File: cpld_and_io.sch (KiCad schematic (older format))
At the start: 3 parts, among them U12 IS61LV5128AL-10TLI, U4 5M1270ZT144C5N

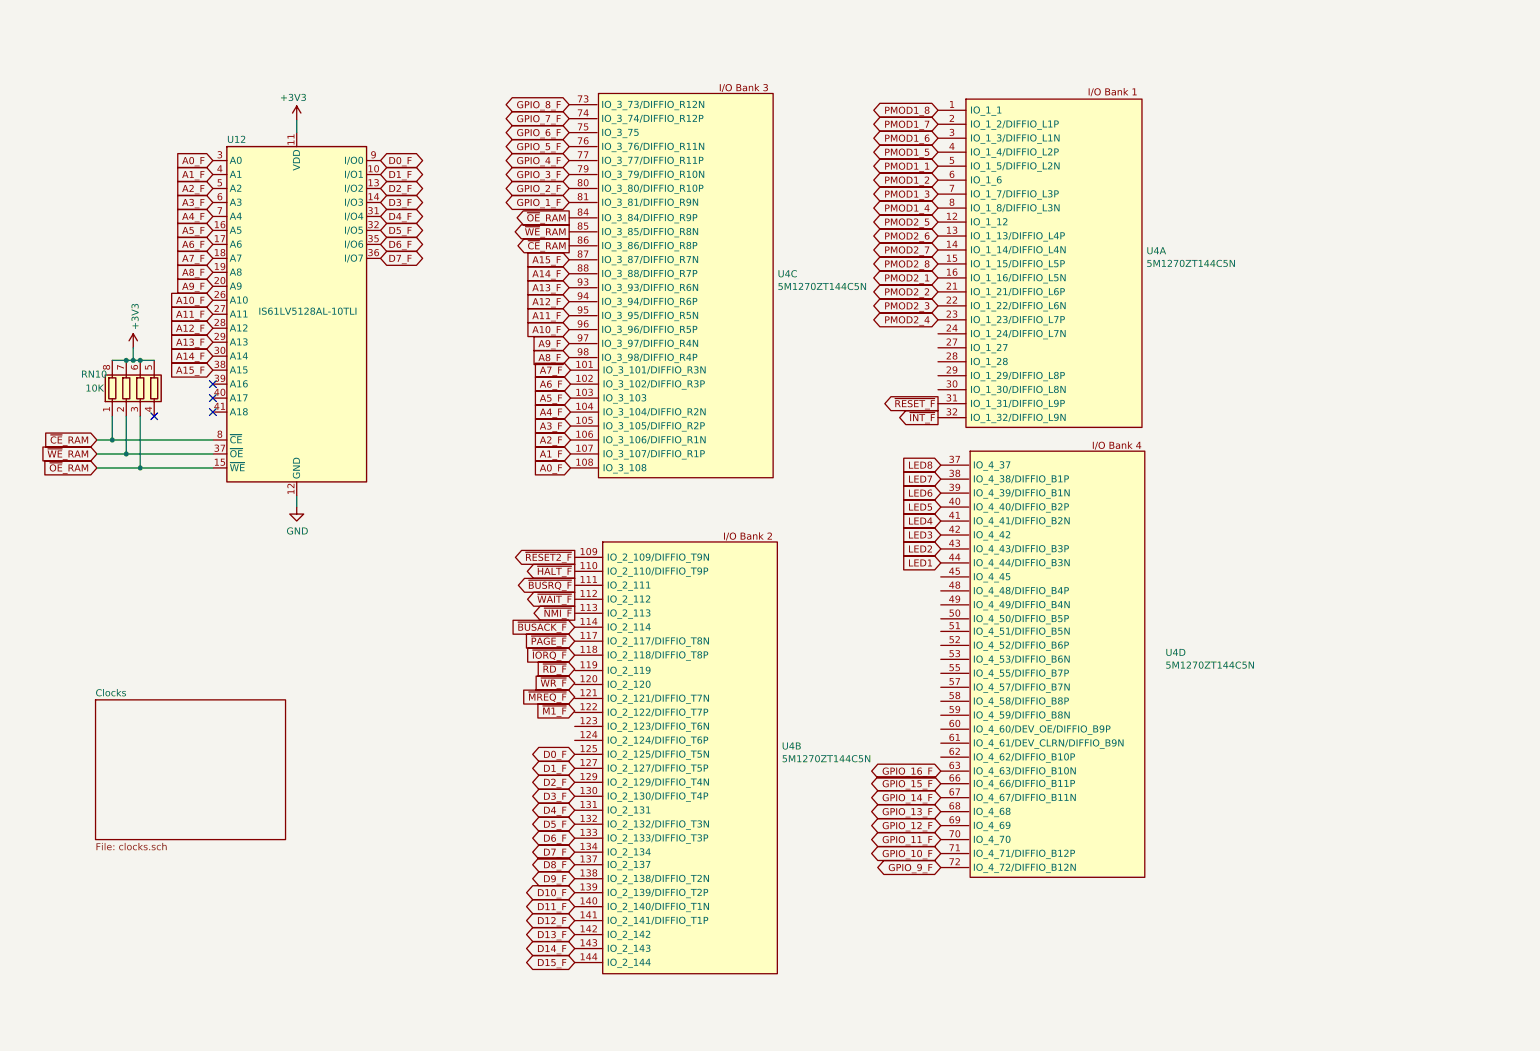
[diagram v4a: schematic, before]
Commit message: fixed errors, connected all pins, switched to 4 layers
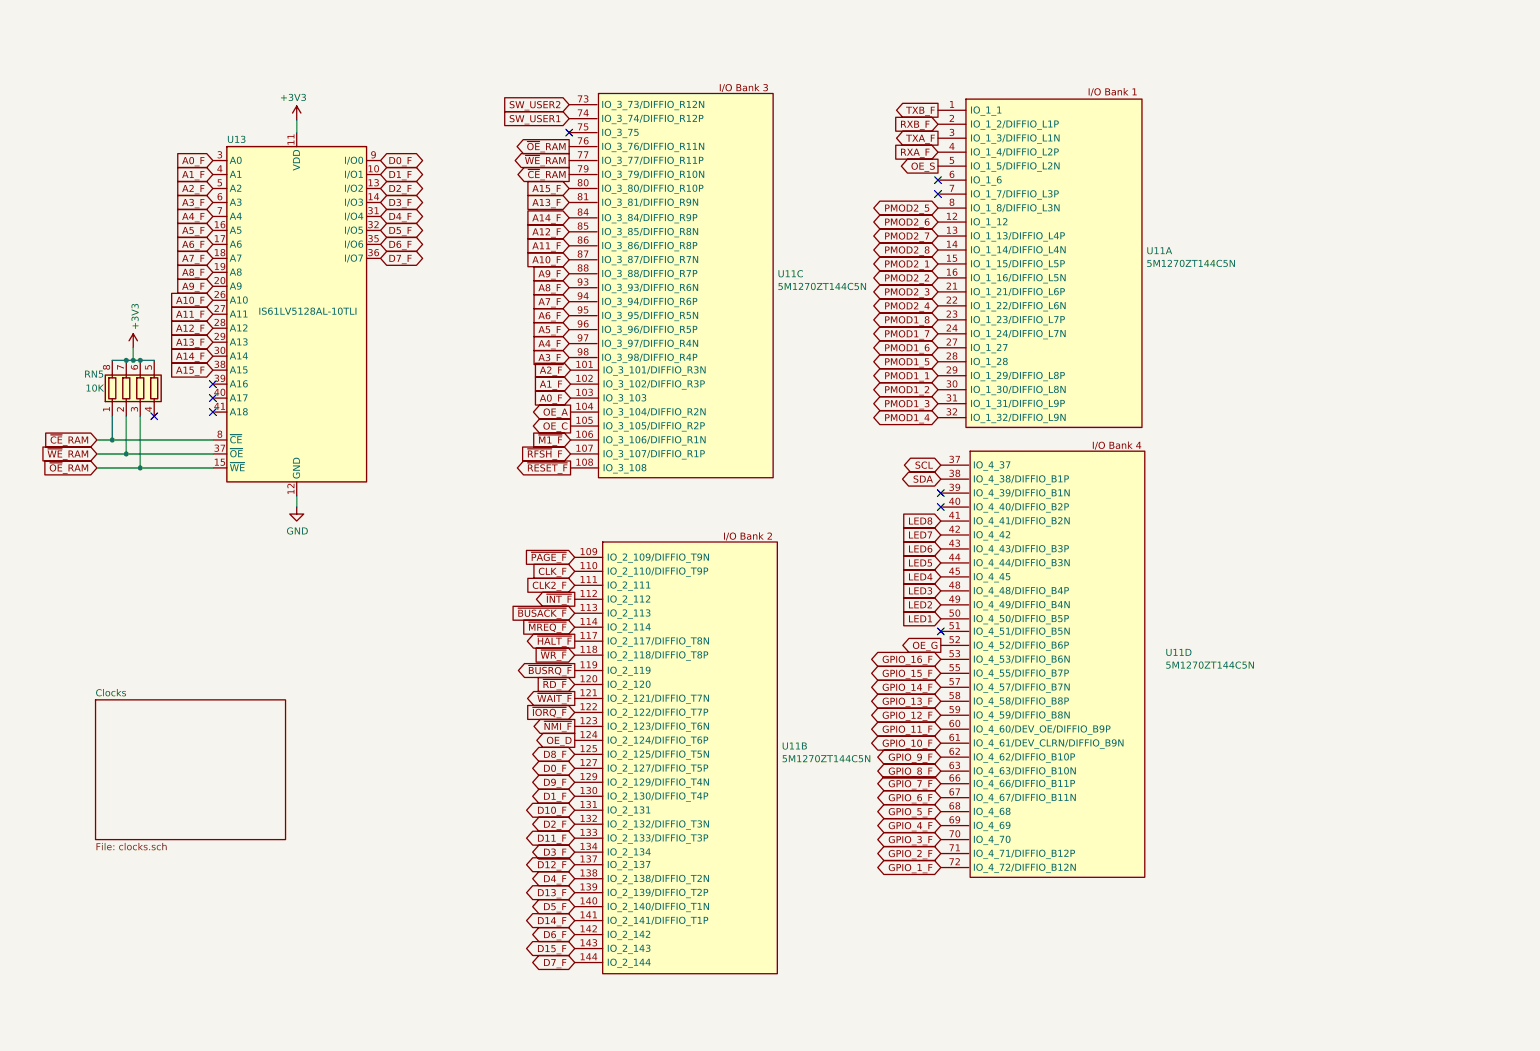
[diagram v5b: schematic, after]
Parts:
- renumbered RN10 to RN5, U4 to U11, U12 to U13
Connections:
- net ~RESET2_F is gone; now on net ~PAGE_F: U11.109 (IO_2_109/DIFFIO_T9N)
- net A0_F: now also U11.103 (IO_3_103); no longer U11.108 (IO_3_108)
- net A10_F: now also U11.87 (IO_3_87/DIFFIO_R7N); no longer U11.96 (IO_3_96/DIFFIO_R5P)
- net A11_F: now also U11.86 (IO_3_86/DIFFIO_R8P); no longer U11.95 (IO_3_95/DIFFIO_R5N)
- net A12_F: now also U11.85 (IO_3_85/DIFFIO_R8N); no longer U11.94 (IO_3_94/DIFFIO_R6P)
- net A13_F: now also U11.81 (IO_3_81/DIFFIO_R9N); no longer U11.93 (IO_3_93/DIFFIO_R6N)
- net A14_F: now also U11.84 (IO_3_84/DIFFIO_R9P); no longer U11.88 (IO_3_88/DIFFIO_R7P)
- net A15_F: now also U11.80 (IO_3_80/DIFFIO_R10P); no longer U11.87 (IO_3_87/DIFFIO_R7N)
- net A1_F: now also U11.102 (IO_3_102/DIFFIO_R3P); no longer U11.107 (IO_3_107/DIFFIO_R1P)
- net A2_F: now also U11.101 (IO_3_101/DIFFIO_R3N); no longer U11.106 (IO_3_106/DIFFIO_R1N)
- net A3_F: now also U11.98 (IO_3_98/DIFFIO_R4P); no longer U11.105 (IO_3_105/DIFFIO_R2P)
- net A4_F: now also U11.97 (IO_3_97/DIFFIO_R4N); no longer U11.104 (IO_3_104/DIFFIO_R2N)
- net A5_F: now also U11.96 (IO_3_96/DIFFIO_R5P); no longer U11.103 (IO_3_103)
- net A6_F: now also U11.95 (IO_3_95/DIFFIO_R5N); no longer U11.102 (IO_3_102/DIFFIO_R3P)
- net A7_F: now also U11.94 (IO_3_94/DIFFIO_R6P); no longer U11.101 (IO_3_101/DIFFIO_R3N)
- net A8_F: now also U11.93 (IO_3_93/DIFFIO_R6N); no longer U11.98 (IO_3_98/DIFFIO_R4P)
- net A9_F: now also U11.88 (IO_3_88/DIFFIO_R7P); no longer U11.97 (IO_3_97/DIFFIO_R4N)
- net D0_F: now also U11.127 (IO_2_127/DIFFIO_T5P); no longer U11.125 (IO_2_125/DIFFIO_T5N)
- net D10_F: now also U11.131 (IO_2_131); no longer U11.139 (IO_2_139/DIFFIO_T2P)
- net D11_F: now also U11.133 (IO_2_133/DIFFIO_T3P); no longer U11.140 (IO_2_140/DIFFIO_T1N)
- net D12_F: now also U11.137 (IO_2_137); no longer U11.141 (IO_2_141/DIFFIO_T1P)
- net D13_F: now also U11.139 (IO_2_139/DIFFIO_T2P); no longer U11.142 (IO_2_142)
- net D14_F: now also U11.141 (IO_2_141/DIFFIO_T1P); no longer U11.143 (IO_2_143)
- net D15_F: now also U11.143 (IO_2_143); no longer U11.144 (IO_2_144)
- net D1_F: now also U11.130 (IO_2_130/DIFFIO_T4P); no longer U11.127 (IO_2_127/DIFFIO_T5P)
- net D2_F: now also U11.132 (IO_2_132/DIFFIO_T3N); no longer U11.129 (IO_2_129/DIFFIO_T4N)
- net D3_F: now also U11.134 (IO_2_134); no longer U11.130 (IO_2_130/DIFFIO_T4P)
- net D4_F: now also U11.138 (IO_2_138/DIFFIO_T2N); no longer U11.131 (IO_2_131)
- net D5_F: now also U11.140 (IO_2_140/DIFFIO_T1N); no longer U11.132 (IO_2_132/DIFFIO_T3N)
- net D6_F: now also U11.142 (IO_2_142); no longer U11.133 (IO_2_133/DIFFIO_T3P)
- net D7_F: now also U11.144 (IO_2_144); no longer U11.134 (IO_2_134)
- net D8_F: now also U11.125 (IO_2_125/DIFFIO_T5N); no longer U11.137 (IO_2_137)
- net D9_F: now also U11.129 (IO_2_129/DIFFIO_T4N); no longer U11.138 (IO_2_138/DIFFIO_T2N)
- net GPIO_10_F: now also U11.61 (IO_4_61/DEV_CLRN/DIFFIO_B9N); no longer U11.71 (IO_4_71/DIFFIO_B12P)
- net GPIO_11_F: now also U11.60 (IO_4_60/DEV_OE/DIFFIO_B9P); no longer U11.70 (IO_4_70)
- net GPIO_12_F: now also U11.59 (IO_4_59/DIFFIO_B8N); no longer U11.69 (IO_4_69)
- net GPIO_13_F: now also U11.58 (IO_4_58/DIFFIO_B8P); no longer U11.68 (IO_4_68)
- net GPIO_14_F: now also U11.57 (IO_4_57/DIFFIO_B7N); no longer U11.67 (IO_4_67/DIFFIO_B11N)
- net GPIO_15_F: now also U11.55 (IO_4_55/DIFFIO_B7P); no longer U11.66 (IO_4_66/DIFFIO_B11P)
- net GPIO_16_F: now also U11.53 (IO_4_53/DIFFIO_B6N); no longer U11.63 (IO_4_63/DIFFIO_B10N)
- net GPIO_1_F: now also U11.72 (IO_4_72/DIFFIO_B12N); no longer U11.81 (IO_3_81/DIFFIO_R9N)
- net GPIO_2_F: now also U11.71 (IO_4_71/DIFFIO_B12P); no longer U11.80 (IO_3_80/DIFFIO_R10P)
- net GPIO_3_F: now also U11.70 (IO_4_70); no longer U11.79 (IO_3_79/DIFFIO_R10N)
- net GPIO_4_F: now also U11.69 (IO_4_69); no longer U11.77 (IO_3_77/DIFFIO_R11P)
- net GPIO_5_F: now also U11.68 (IO_4_68); no longer U11.76 (IO_3_76/DIFFIO_R11N)
- net GPIO_6_F: now also U11.67 (IO_4_67/DIFFIO_B11N); no longer U11.75 (IO_3_75)
- net GPIO_7_F: now also U11.66 (IO_4_66/DIFFIO_B11P); no longer U11.74 (IO_3_74/DIFFIO_R12P)
- net GPIO_8_F: now also U11.63 (IO_4_63/DIFFIO_B10N); no longer U11.73 (IO_3_73/DIFFIO_R12N)
- net GPIO_9_F: now also U11.62 (IO_4_62/DIFFIO_B10P); no longer U11.72 (IO_4_72/DIFFIO_B12N)
- net LED1: now also U11.50 (IO_4_50/DIFFIO_B5P); no longer U11.44 (IO_4_44/DIFFIO_B3N)
- net LED2: now also U11.49 (IO_4_49/DIFFIO_B4N); no longer U11.43 (IO_4_43/DIFFIO_B3P)
- net LED3: now also U11.48 (IO_4_48/DIFFIO_B4P); no longer U11.42 (IO_4_42)
- net LED4: now also U11.45 (IO_4_45); no longer U11.41 (IO_4_41/DIFFIO_B2N)
- net LED5: now also U11.44 (IO_4_44/DIFFIO_B3N); no longer U11.40 (IO_4_40/DIFFIO_B2P)
- net LED6: now also U11.43 (IO_4_43/DIFFIO_B3P); no longer U11.39 (IO_4_39/DIFFIO_B1N)
- net LED7: now also U11.42 (IO_4_42); no longer U11.38 (IO_4_38/DIFFIO_B1P)
- net LED8: now also U11.41 (IO_4_41/DIFFIO_B2N); no longer U11.37 (IO_4_37)
- net PMOD1_1: now also U11.29 (IO_1_29/DIFFIO_L8P); no longer U11.5 (IO_1_5/DIFFIO_L2N)
- net PMOD1_2: now also U11.30 (IO_1_30/DIFFIO_L8N); no longer U11.6 (IO_1_6)
- net PMOD1_3: now also U11.31 (IO_1_31/DIFFIO_L9P); no longer U11.7 (IO_1_7/DIFFIO_L3P)
- net PMOD1_4: now also U11.32 (IO_1_32/DIFFIO_L9N); no longer U11.8 (IO_1_8/DIFFIO_L3N)
- net PMOD1_5: now also U11.28 (IO_1_28); no longer U11.4 (IO_1_4/DIFFIO_L2P)
- net PMOD1_6: now also U11.27 (IO_1_27); no longer U11.3 (IO_1_3/DIFFIO_L1N)
- net PMOD1_7: now also U11.24 (IO_1_24/DIFFIO_L7N); no longer U11.2 (IO_1_2/DIFFIO_L1P)
- net PMOD1_8: now also U11.23 (IO_1_23/DIFFIO_L7P); no longer U11.1 (IO_1_1)
- net PMOD2_1: now also U11.15 (IO_1_15/DIFFIO_L5P); no longer U11.16 (IO_1_16/DIFFIO_L5N)
- net PMOD2_2: now also U11.16 (IO_1_16/DIFFIO_L5N); no longer U11.21 (IO_1_21/DIFFIO_L6P)
- net PMOD2_3: now also U11.21 (IO_1_21/DIFFIO_L6P); no longer U11.22 (IO_1_22/DIFFIO_L6N)
- net PMOD2_4: now also U11.22 (IO_1_22/DIFFIO_L6N); no longer U11.23 (IO_1_23/DIFFIO_L7P)
- net PMOD2_5: now also U11.8 (IO_1_8/DIFFIO_L3N); no longer U11.12 (IO_1_12)
- net PMOD2_6: now also U11.12 (IO_1_12); no longer U11.13 (IO_1_13/DIFFIO_L4P)
- net PMOD2_7: now also U11.13 (IO_1_13/DIFFIO_L4P); no longer U11.14 (IO_1_14/DIFFIO_L4N)
- net PMOD2_8: now also U11.14 (IO_1_14/DIFFIO_L4N); no longer U11.15 (IO_1_15/DIFFIO_L5P)
- net ~BUSACK_F: now also U11.113 (IO_2_113); no longer U11.114 (IO_2_114)
- net ~BUSRQ_F: now also U11.119 (IO_2_119); no longer U11.111 (IO_2_111)
- net ~CE~_RAM: now also U11.79 (IO_3_79/DIFFIO_R10N); no longer U11.86 (IO_3_86/DIFFIO_R8P)
- net ~HALT_F: now also U11.117 (IO_2_117/DIFFIO_T8N); no longer U11.110 (IO_2_110/DIFFIO_T9P)
- net ~INT_F: now also U11.112 (IO_2_112); no longer U11.32 (IO_1_32/DIFFIO_L9N)
- net ~IORQ_F: now also U11.122 (IO_2_122/DIFFIO_T7P); no longer U11.118 (IO_2_118/DIFFIO_T8P)
- net ~M1_F: now also U11.106 (IO_3_106/DIFFIO_R1N)
- net ~MREQ_F: now also U11.114 (IO_2_114)
- net ~NMI_F: now also U11.123 (IO_2_123/DIFFIO_T6N); no longer U11.113 (IO_2_113)
- net ~OE~_RAM: now also U11.76 (IO_3_76/DIFFIO_R11N); no longer U11.84 (IO_3_84/DIFFIO_R9P)
- net ~PAGE_F: no longer U11.117 (IO_2_117/DIFFIO_T8N)
- net ~RD_F: now also U11.120 (IO_2_120)
- net ~RESET_F: now also U11.108 (IO_3_108); no longer U11.31 (IO_1_31/DIFFIO_L9P)
- net ~WAIT_F: now also U11.121 (IO_2_121/DIFFIO_T7N); no longer U11.112 (IO_2_112)
- net ~WE~_RAM: now also U11.77 (IO_3_77/DIFFIO_R11P); no longer U11.85 (IO_3_85/DIFFIO_R8N)
- net ~WR_F: now also U11.118 (IO_2_118/DIFFIO_T8P)
- net OE_D: now reaches U11.124 (IO_2_124/DIFFIO_T6P)
- net OE_G: now reaches U11.52 (IO_4_52/DIFFIO_B6P)
- new net CLK2_F: U11.111 (IO_2_111)
- new net CLK_F: U11.110 (IO_2_110/DIFFIO_T9P)
- new net OE_A: U11.104 (IO_3_104/DIFFIO_R2N)
- new net OE_C: U11.105 (IO_3_105/DIFFIO_R2P)
- new net OE_S: U11.5 (IO_1_5/DIFFIO_L2N)
- new net RXA_F: U11.4 (IO_1_4/DIFFIO_L2P)
- new net RXB_F: U11.2 (IO_1_2/DIFFIO_L1P)
- new net SCL: U11.37 (IO_4_37)
- new net SDA: U11.38 (IO_4_38/DIFFIO_B1P)
- new net SW_USER1: U11.74 (IO_3_74/DIFFIO_R12P)
- new net SW_USER2: U11.73 (IO_3_73/DIFFIO_R12N)
- new net TXA_F: U11.3 (IO_1_3/DIFFIO_L1N)
- new net TXB_F: U11.1 (IO_1_1)
- new net ~RFSH~_F: U11.107 (IO_3_107/DIFFIO_R1P)
- no-connect marks 4 -> 10

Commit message: Updated BOM
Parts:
- RN5: MFR (none) -> Panasonic; MPN (none) -> EXB-38V103JV; SPR (none) -> Mouser
- U11: MFR (none) -> Intel; MPN (none) -> 5M1270ZT144C5N; Manufacturer_Name Intel -> (none); SPR (none) -> Mouser
- U13: MFR (none) -> ISSI; MPN (none) -> IS61LV5128AL-10TLI; SPR (none) -> Mouser
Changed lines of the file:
@@
 F 2 "Package_SO:TSOP-II-44_10.16x18.41mm_P0.8mm" H 1930 3400 50  0001 C CNN
 F 3 "http://www.issi.com/WW/pdf/61-64C5128AL.pdf" H 2430 2250 50  0001 C CNN
+F 4 "ISSI" H 2430 2250 50  0001 C CNN "MFR"
+F 5 "IS61LV5128AL-10TLI" H 2430 2250 50  0001 C CNN "MPN"
+F 6 "Mouser" H 2430 2250 50  0001 C CNN "SPR"
 	1    2430 2250
 	1    0    0    -1
@@
 F 4 "CPLD - Complex Programmable Logic Devices CPLD - MAX V 980 Macro 114 IOs" H 9690 3420 50  0001 L CNN "Description"
 F 5 "1.55" H 9690 3320 50  0001 L CNN "Height"
-F 6 "Intel" H 9690 3020 50  0001 L CNN "Manufacturer_Name"
-F 7 "5M1270ZT144C5N" H 9690 2920 50  0001 L CNN "Manufacturer_Part_Number"
+F 6 "5M1270ZT144C5N" H 9690 2920 50  0001 L CNN "Manufacturer_Part_Number"
+F 7 "Intel" H 7850 720 50  0001 C CNN "MFR"
+F 8 "5M1270ZT144C5N" H 7850 720 50  0001 C CNN "MPN"
+F 9 "Mouser" H 7850 720 50  0001 C CNN "SPR"
 	1    7850 720
 	1    0    0    -1
@@
 F 4 "CPLD - Complex Programmable Logic Devices CPLD - MAX V 980 Macro 114 IOs" H 7080 6590 50  0001 L CNN "Description"
 F 5 "1.55" H 7080 6490 50  0001 L CNN "Height"
-F 6 "Intel" H 7080 6190 50  0001 L CNN "Manufacturer_Name"
-F 7 "5M1270ZT144C5N" H 7080 6090 50  0001 L CNN "Manufacturer_Part_Number"
+F 6 "5M1270ZT144C5N" H 7080 6090 50  0001 L CNN "Manufacturer_Part_Number"
+F 7 "Intel" H 5240 3890 50  0001 C CNN "MFR"
+F 8 "5M1270ZT144C5N" H 5240 3890 50  0001 C CNN "MPN"
+F 9 "Mouser" H 5240 3890 50  0001 C CNN "SPR"
 	2    5240 3890
 	1    0    0    -1
@@
 F 4 "CPLD - Complex Programmable Logic Devices CPLD - MAX V 980 Macro 114 IOs" H 7050 3370 50  0001 L CNN "Description"
 F 5 "1.55" H 7050 3270 50  0001 L CNN "Height"
-F 6 "Intel" H 7050 2970 50  0001 L CNN "Manufacturer_Name"
-F 7 "5M1270ZT144C5N" H 7050 2870 50  0001 L CNN "Manufacturer_Part_Number"
+F 6 "5M1270ZT144C5N" H 7050 2870 50  0001 L CNN "Manufacturer_Part_Number"
+F 7 "Intel" H 5210 670 50  0001 C CNN "MFR"
+F 8 "5M1270ZT144C5N" H 5210 670 50  0001 C CNN "MPN"
+F 9 "Mouser" H 5210 670 50  0001 C CNN "SPR"
 	3    5210 670
 	1    0    0    -1
@@
 F 4 "CPLD - Complex Programmable Logic Devices CPLD - MAX V 980 Macro 114 IOs" H 9720 5930 50  0001 L CNN "Description"
 F 5 "1.55" H 9720 5830 50  0001 L CNN "Height"
-F 6 "Intel" H 9720 5530 50  0001 L CNN "Manufacturer_Name"
-F 7 "5M1270ZT144C5N" H 9720 5430 50  0001 L CNN "Manufacturer_Part_Number"
+F 6 "5M1270ZT144C5N" H 9720 5430 50  0001 L CNN "Manufacturer_Part_Number"
+F 7 "Intel" H 7880 3230 50  0001 C CNN "MFR"
+F 8 "5M1270ZT144C5N" H 7880 3230 50  0001 C CNN "MPN"
+F 9 "Mouser" H 7880 3230 50  0001 C CNN "SPR"
 	4    7880 3230
 	1    0    0    -1
@@
 F 2 "Resistor_SMD:R_Array_Concave_4x0603" V 1585 2780 50  0001 C CNN
 F 3 "~" H 1310 2780 50  0001 C CNN
+F 4 "Panasonic" H 1310 2780 50  0001 C CNN "MFR"
+F 5 "EXB-38V103JV" H 1310 2780 50  0001 C CNN "MPN"
+F 6 "Mouser" H 1310 2780 50  0001 C CNN "SPR"
 	1    1310 2780
 	1    0    0    -1

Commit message: updated descriptions and part #'s
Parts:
- RN5: Description (none) -> Resistor Networks & Arrays 10K OHM 5%; SPN (none) -> 667-EXB-38V103JV; SPURL (none) -> https://www.mouser.com/ProductDetail/667-EXB-38V103JV
- U11: SPN (none) -> 989-5M1270ZT144C5N; SPURL (none) -> https://www.mouser.com/ProductDetail/989-5M1270ZT144C5N
- U13: Description (none) -> SRAM 4Mb 512Kx8 10ns Async SRAM 3.3v; SPN (none) -> 870IS61LV5128AL10TLI; SPURL (none) -> https://www.mouser.com/ProductDetail/870IS61LV5128AL10TLI
